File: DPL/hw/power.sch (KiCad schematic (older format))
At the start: 9 parts, among them U2 AP7215-33YG-13

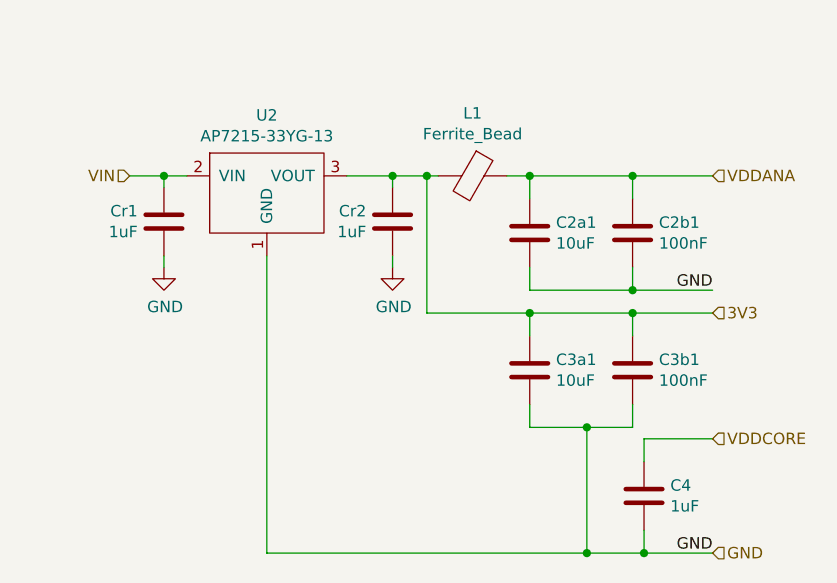
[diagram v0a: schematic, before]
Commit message: Started new design of the DPL payload.
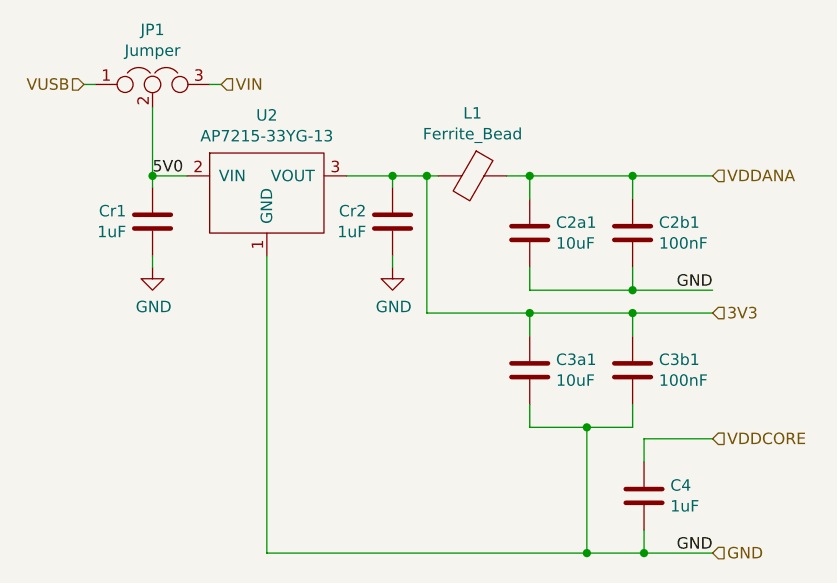
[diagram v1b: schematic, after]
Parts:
- added JP1: Jumper, Connector_PinHeader_2.54mm:PinHeader_1x03_P2.54mm_Vertical, symbol Device:Jumper_NC_Dual
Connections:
- net VIN: now also JP1.3; no longer Cr1.1, U2.2 (VIN)
- new net 5V0: Cr1.1, JP1.2, U2.2 (VIN)
- new net VUSB: JP1.1
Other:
- moved on the sheet: Cr1
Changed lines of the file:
@@
 EESchema Schematic File Version 5
 LIBS:DPL-cache
-EELAYER 29 0
+EELAYER 30 0
 EELAYER END
 $Descr A4 11693 8268
 encoding utf-8
-Sheet 3 3
+Sheet 2 5
 Title ""
 Date ""
@@
 Comment3 ""
 Comment4 ""
+Comment5 ""
+Comment6 ""
+Comment7 ""
+Comment8 ""
+Comment9 ""
 $EndDescr
 $Comp
@@
 	5400 4000 5050 4000
 Connection ~ 5050 4000
-Text HLabel 2850 3400 0    50   Input ~ 0
-VIN
 $Comp
 L Device:C Cr1
 U 1 1 5BB30701
-P 3000 3600
-F 0 "Cr1" H 3115 3646 50  0000 L CNN
-F 1 "1uF" H 3115 3555 50  0000 L CNN
-F 2 "Capacitor_SMD:C_0603_1608Metric_Pad1.05x0.95mm_HandSolder" H 3038 3450 50  0001 C CNN
-F 3 "~" H 3000 3600 50  0001 C CNN
-	1    3000 3600
+P 2950 3600
+F 0 "Cr1" H 3065 3646 50  0000 L CNN
+F 1 "1uF" H 3065 3555 50  0000 L CNN
+F 2 "Capacitor_SMD:C_0603_1608Metric_Pad1.05x0.95mm_HandSolder" H 2988 3450 50  0001 C CNN
+F 3 "~" H 2950 3600 50  0001 C CNN
+	1    2950 3600
 	-1   0    0    -1
 $EndComp
@@
 	4000 3400 4150 3400
 Wire Wire Line
-	2850 3400 3000 3400
-Wire Wire Line
-	3000 3450 3000 3400
-Connection ~ 3000 3400
-Wire Wire Line
-	3000 3400 3100 3400
-Wire Wire Line
-	3000 3750 3000 3800
+	2950 3450 2950 3400
+Wire Wire Line
+	2950 3750 2950 3800
 Wire Wire Line
 	4000 3750 4000 3800
@@
 L power:GND #PWR0107
 U 1 1 5BB332C0
-P 3000 3800
-F 0 "#PWR0107" H 3000 3550 50  0001 C CNN
-F 1 "GND" H 3005 3627 50  0000 C CNN
-F 2 "" H 3000 3800 50  0001 C CNN
-F 3 "" H 3000 3800 50  0001 C CNN
-	1    3000 3800
+P 2950 3800
+F 0 "#PWR0107" H 2950 3550 50  0001 C CNN
+F 1 "GND" H 2955 3627 50  0000 C CNN
+F 2 "" H 2950 3800 50  0001 C CNN
+F 3 "" H 2950 3800 50  0001 C CNN
+	1    2950 3800
 	1    0    0    -1
 $EndComp
@@
 Wire Wire Line
 	3450 5050 3450 3750
+Text HLabel 2650 3000 0    50   Input ~ 0
+VUSB
+Text Label 2950 3400 0    50   ~ 0
+5V0
+Wire Wire Line
+	2950 3400 3100 3400
+$Comp
+L Device:Jumper_NC_Dual JP1
+U 1 1 5D23AF9C
+P 2950 3000
+F 0 "JP1" H 2950 3239 50  0000 C CNN
+F 1 "Jumper" H 2950 3148 50  0000 C CNN
+F 2 "Connector_PinHeader_2.54mm:PinHeader_1x03_P2.54mm_Vertical" H 2950 3000 50  0001 C CNN
+F 3 "~" H 2950 3000 50  0001 C CNN
+	1    2950 3000
+	1    0    0    -1
+$EndComp
+Text HLabel 3250 3000 2    50   Input ~ 0
+VIN
+Wire Wire Line
+	3250 3000 3200 3000
+Wire Wire Line
+	2700 3000 2650 3000
+Wire Wire Line
+	2950 3100 2950 3400
+Connection ~ 2950 3400
 Wire Wire Line
 	3450 5050 4850 5050
